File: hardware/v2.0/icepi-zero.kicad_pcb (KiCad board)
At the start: 4 copper layers, 65 x 30 mm, 208 parts, among them IC1 IS42S16160J-6BLI, IC2 LTC2256CUJ-12#PBF, IC3 LTC2630ISC6-LZ12#TRMPBF, J1 Conn_02x20_Counter_Clockwise, J2 GPDI_C_1.3, J3 USB_C_Receptacle_USB2.0_14P, J4 USB_C_Receptacle_USB2.0_14P, J5 USB_C_Receptacle_USB2.0_14P, J6 Micro_SD_Card_Det2, J7 RSP-122811-01, J8 530480210, SW1 SW_Push, SW2 SW_Push, U1 ECP5U-25F-CABGA256, U10 TPD2EUSB30A, U11 LT1993CUD-2_PBF, U12 W25Q128JVS, U13 TCR5FM50A, U2 LTC3407AEDD-2_PBF, U3 TLV62569DBV, U5 TCR5FM18A, U6 PCA9306DC1, U7 TPD2EUSB30A, U8 TPD2EUSB30A, U9 FT231XQ, Y1 SG-8018CG 50.000000MHz, Y2 SG-8018CG 25.000000MHz

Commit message: 2CH DAC
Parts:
- removed IC3: LTC2630ISC6-LZ12#TRMPBF, LTC2630ISC6-LZ12#TRMPBF:SOT65P210X100-6N
- added IC4: LTC2622IMS8#PBF, LTC2622IMS8#PBF:SOP65P490X110-8N, B.Cu at (178.0, 101.2)
- J8: value 530480210 -> BM04B-ACHSS-A-GAN-TFLFSN; footprint 530480210:MOLEX_530480210 -> BM04B_ACHSS_A_GAN_TF_LF__SN:BM04B-ACHSS-A-GAN-TFLFSN_JST
- moved C82 7.79 mm to (183.3, 106.8), turned to 0 degrees
- moved C62 3.84 mm to (174.0, 96.3), turned to 90 degrees
- moved J8 1.68 mm to (178.3, 110.1), turned to 90 degrees
- moved C55 1.08 mm to (177.4, 105.8), turned to 180 degrees
- moved C60 0.65 mm to (175.0, 106.9), turned to 90 degrees
- moved C69 0.27 mm to (173.7, 107.3)
- moved R56 0.10 mm to (175.7, 104.9)
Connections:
- J8 pad 1: /DAC/VOUT(DAC) -> +3V3
- J8 pad 2: GND -> /DAC/VOUT_A
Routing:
- net /DAC/VOUT_B: track 0.00 -> 16.6 mm
- net /DAC/VOUT_A: track 0.00 -> 12.3 mm
- net /DAC/VOUT(DAC): track 8.02 -> 0.00 mm
- net SCK: track 33.4 -> 36.7 mm
- net GND: track 97.7 -> 99.7 mm, vias 111 -> 112
- net /DAC/~{CS}(DAC): track 27.5 -> 29.4 mm
- net +3V3: track 126.7 -> 125.3 mm, vias 33 -> 32
- net /SW1: track 33.7 -> 34.7 mm
- net SDI: track 35.7 -> 36.7 mm
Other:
- board text removed: "Vout"
- board text removed: "⏚"

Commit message: DRC pass
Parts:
- moved C82 10.5 mm to (178.4, 97.5)
- moved C25 0.10 mm to (147.8, 101.7)
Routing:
- net +3V3: track 125.3 -> 128.9 mm, vias 32 -> 33
- net /DAC/VOUT_B: track 16.6 -> 16.1 mm

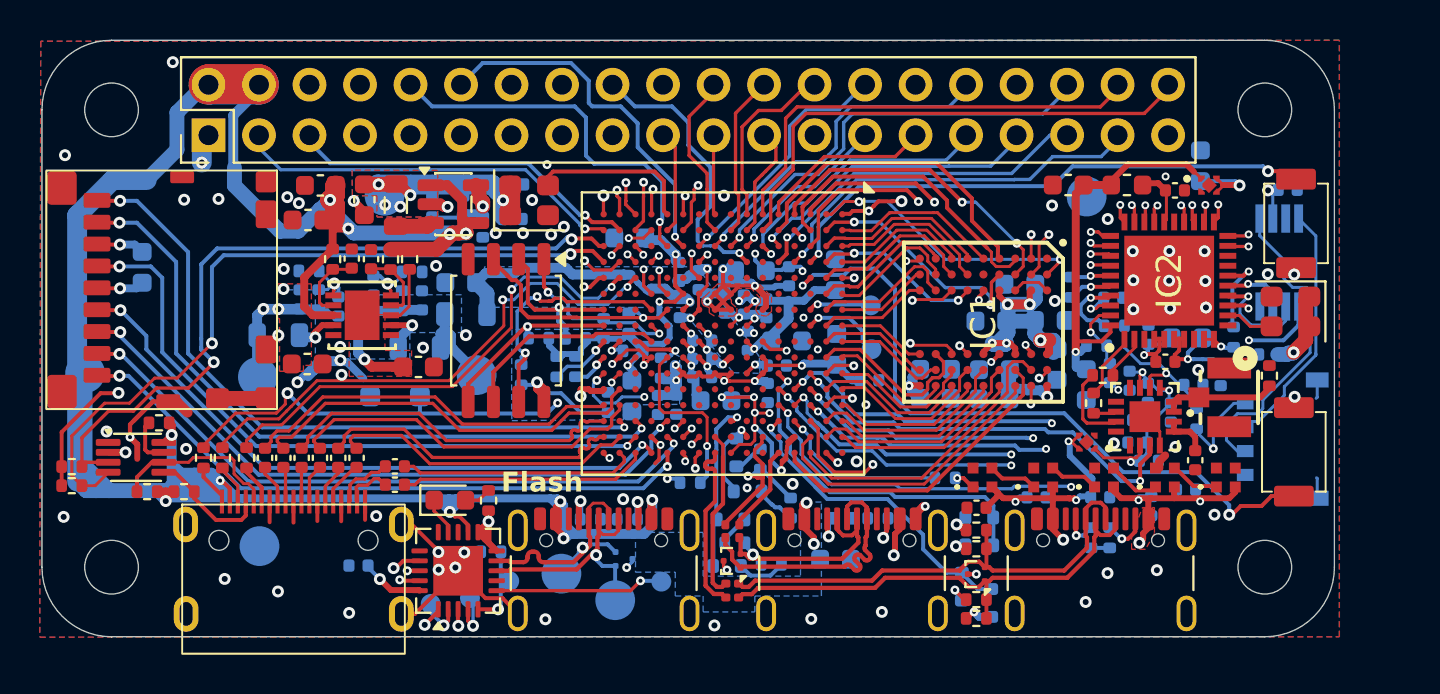
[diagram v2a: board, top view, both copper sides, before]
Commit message: Impedance control 100Ohm ADC LVDS diff pairs
Calculated for PCBWay 92th stack with 1OZ inner copper layer
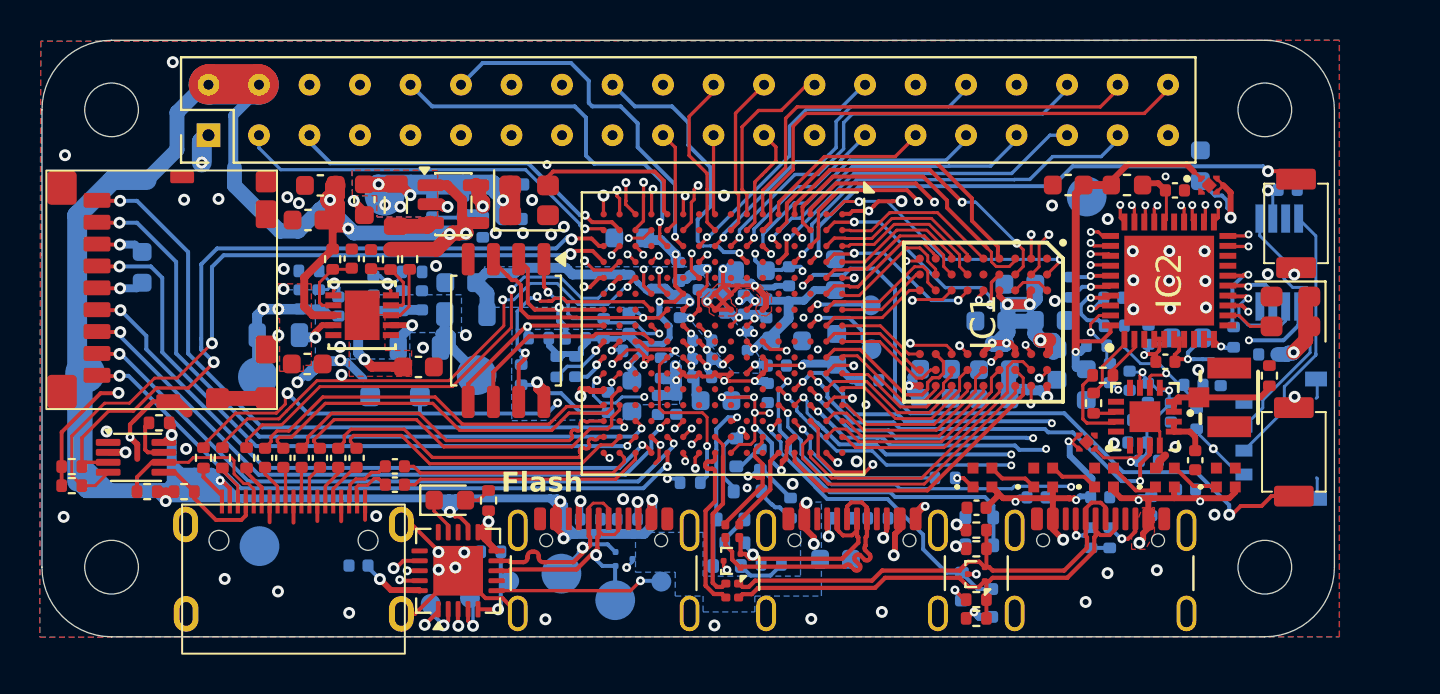
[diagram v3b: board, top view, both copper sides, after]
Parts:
- J8: value BM04B-ACHSS-A-GAN-TFLFSN -> BM04B-ACHSS-A-GAN-TF_LF__SN_; footprint BM04B_ACHSS_A_GAN_TF_LF__SN:BM04B-ACHSS-A-GAN-TFLFSN_JST -> BM04B_ACHSS_A_GAN_TF_LF__SN:BM04BACHSSAGANTFLFSN
- moved J8 0.43 mm to (177.9, 110.0), turned to 0 degrees
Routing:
- net /DAC/VOUT_B: track 16.1 -> 13.3 mm
- net /DAC/VOUT_A: track 12.6 -> 13.6 mm
